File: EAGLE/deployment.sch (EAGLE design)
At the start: 7 parts, among them J1 1935161, J2 1935161, J3 1935161, Q1 100V 14A

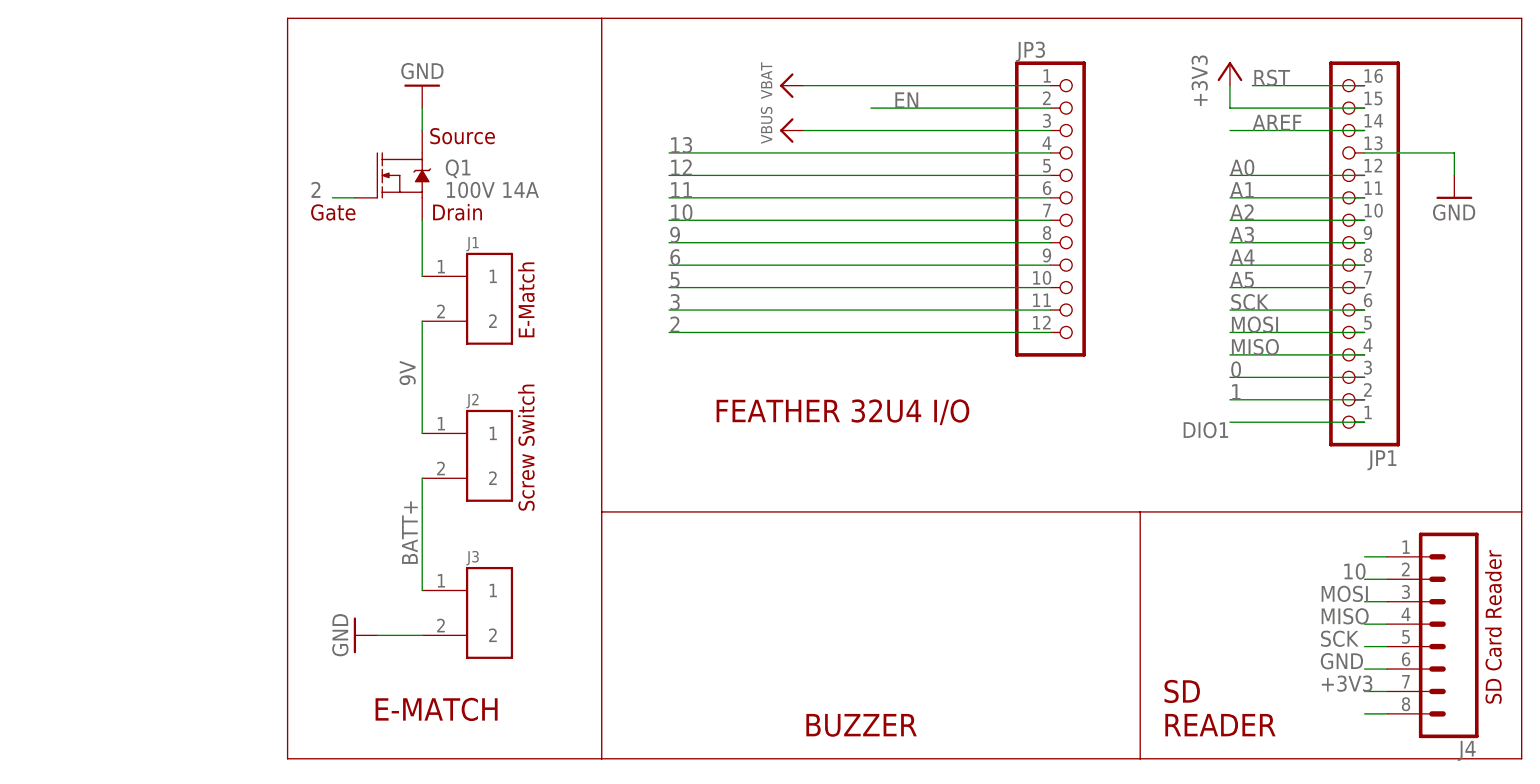
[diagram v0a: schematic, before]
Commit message: Added nichrome wire circuit to deployment schematic
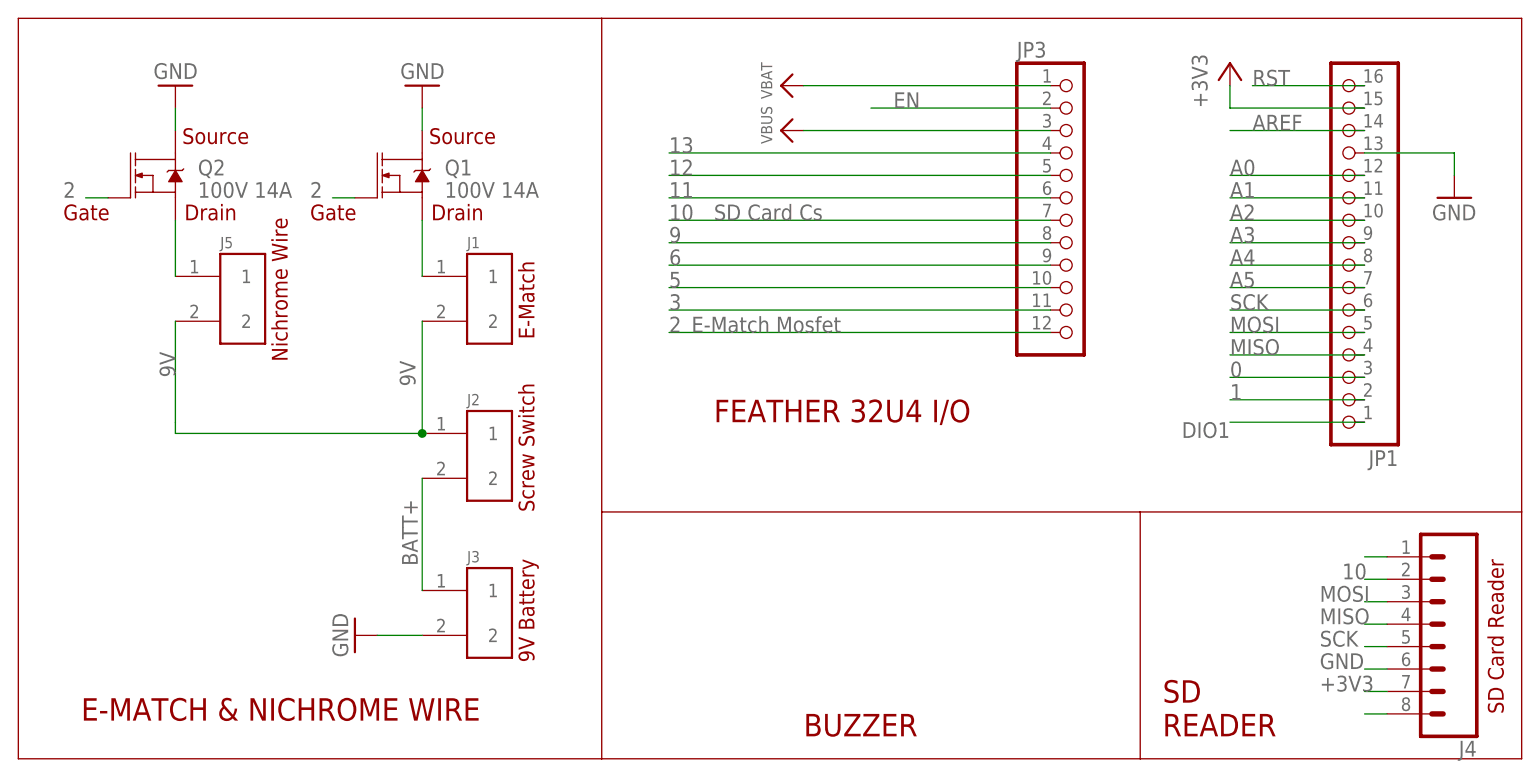
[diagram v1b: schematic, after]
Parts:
- added J5: 1935161, 1935161:1935161
- added Q2: 100V 14A, SparkFun-DiscreteSemi:MOSFET-NCH-FQP30N06L
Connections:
- new net N$2: J5.1, Q2.S
- net 2: now also Q2.G
- net 9V: now also J5.2
- net GND: now also Q2.D
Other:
- note added: "9V Battery"
- note added: "E-MATCH & NICHROME WIRE"
- note added: "E-Match Mosfet"
- note added: "Nichrome Wire"
- note added: "SD Card Cs"
- note removed: "E-MATCH"
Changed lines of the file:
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@@
 <part name="GND2" library="supply1" deviceset="GND" device=""/>
 <part name="J4" library="SparkFun-Connectors" library_urn="urn:adsk.eagle:library:513" deviceset="CONN_08" device="&quot;" package3d_urn="urn:adsk.eagle:package:38138/1"/>
+<part name="Q2" library="SparkFun-DiscreteSemi" library_urn="urn:adsk.eagle:library:514" deviceset="MOSFET-NCH" device="-FQP30N06L" package3d_urn="urn:adsk.eagle:package:38447/1" value="100V 14A"/>
+<part name="J5" library="1935161" deviceset="1935161" device="" value=""/>
+<part name="GND3" library="supply1" deviceset="GND" device=""/>
 </parts>
 <sheets>
@@
 <text x="58.42" y="55.118" size="1.778" layer="94" rot="R90">E-Match</text>
 <text x="58.42" y="35.56" size="1.778" layer="94" rot="R90">Screw Switch</text>
-<text x="167.894" y="13.716" size="1.778" layer="94" rot="R90">SD Card Reader</text>
+<text x="168.148" y="12.7" size="1.778" layer="94" rot="R90">SD Card Reader</text>
 <wire x1="170.18" y1="35.56" x2="170.18" y2="7.62" width="0.1524" layer="94"/>
 <wire x1="170.18" y1="7.62" x2="127" y2="7.62" width="0.1524" layer="94"/>
 <wire x1="127" y1="7.62" x2="127" y2="35.56" width="0.1524" layer="94"/>
 <wire x1="127" y1="7.62" x2="66.04" y2="7.62" width="0.1524" layer="94"/>
-<wire x1="66.04" y1="7.62" x2="30.48" y2="7.62" width="0.1524" layer="94"/>
-<wire x1="30.48" y1="7.62" x2="30.48" y2="91.44" width="0.1524" layer="94"/>
-<wire x1="30.48" y1="91.44" x2="66.04" y2="91.44" width="0.1524" layer="94"/>
+<wire x1="66.04" y1="7.62" x2="0" y2="7.62" width="0.1524" layer="94"/>
+<wire x1="0" y1="7.62" x2="0" y2="91.44" width="0.1524" layer="94"/>
+<wire x1="0" y1="91.44" x2="66.04" y2="91.44" width="0.1524" layer="94"/>
 <wire x1="66.04" y1="35.56" x2="66.04" y2="7.62" width="0.1524" layer="94"/>
-<text x="40.132" y="11.938" size="2.54" layer="94">E-MATCH</text>
+<text x="7.112" y="11.938" size="2.54" layer="94">E-MATCH &amp; NICHROME WIRE</text>
 <text x="78.74" y="45.72" size="2.54" layer="94">FEATHER 32U4 I/O</text>
 <text x="129.54" y="10.16" size="2.54" layer="94">SD
 READER</text>
 <text x="88.9" y="10.16" size="2.54" layer="94">BUZZER</text>
+<text x="58.42" y="18.542" size="1.778" layer="94" rot="R90">9V Battery</text>
+<text x="76.2" y="55.88" size="1.778" layer="95">E-Match Mosfet</text>
+<text x="78.74" y="68.58" size="1.778" layer="95">SD Card Cs</text>
+<text x="5.08" y="68.58" size="1.778" layer="94">Gate</text>
+<text x="18.542" y="77.216" size="1.778" layer="94">Source</text>
+<text x="18.796" y="68.58" size="1.778" layer="94">Drain</text>
+<text x="30.48" y="52.578" size="1.778" layer="94" rot="R90">Nichrome Wire</text>
 </plain>
 <instances>
@@
 <attribute name="VALUE" x="165.1" y="35.306" size="1.778" layer="96" font="vector" rot="R180"/>
 <attribute name="NAME" x="165.1" y="9.652" size="1.778" layer="95" font="vector" rot="R180"/>
+</instance>
+<instance part="Q2" gate="NMOS" x="15.24" y="73.66" smashed="yes">
+<attribute name="NAME" x="20.32" y="73.66" size="1.778" layer="95" font="vector"/>
+<attribute name="VALUE" x="20.32" y="71.12" size="1.778" layer="96" font="vector"/>
+</instance>
+<instance part="J5" gate="G$1" x="25.4" y="59.69" smashed="yes">
+<attribute name="NAME" x="22.85451875" y="65.417340625" size="1.272740625" layer="95"/>
+<attribute name="VALUE" x="22.85191875" y="52.04576875" size="1.274040625" layer="96"/>
+</instance>
+<instance part="GND3" gate="1" x="17.78" y="83.82" smashed="yes" rot="R180">
+<attribute name="VALUE" x="20.32" y="86.36" size="1.778" layer="96" rot="R180"/>
 </instance>
 </instances>
@@
 <label x="147.32" y="17.78" size="1.778" layer="95"/>
 </segment>
+<segment>
+<pinref part="GND3" gate="1" pin="GND"/>
+<pinref part="Q2" gate="NMOS" pin="D"/>
+<wire x1="17.78" y1="81.28" x2="17.78" y2="78.74" width="0.1524" layer="91"/>
+</segment>
 </net>
 <net name="MOSI" class="0">
@@
 <wire x1="38.1" y1="71.12" x2="35.56" y2="71.12" width="0.1524" layer="91"/>
 <label x="33.02" y="71.12" size="1.778" layer="95"/>
+</segment>
+<segment>
+<pinref part="Q2" gate="NMOS" pin="G"/>
+<wire x1="10.16" y1="71.12" x2="7.62" y2="71.12" width="0.1524" layer="91"/>
+<label x="5.08" y="71.12" size="1.778" layer="95"/>
 </segment>
 </net>
@@
 <wire x1="45.72" y1="57.15" x2="45.72" y2="44.45" width="0.1524" layer="91"/>
 <label x="44.958" y="49.784" size="1.778" layer="95" rot="R90"/>
+<pinref part="J5" gate="G$1" pin="2"/>
+<wire x1="17.78" y1="57.15" x2="17.78" y2="45.72" width="0.1524" layer="91"/>
+<wire x1="45.72" y1="44.45" x2="17.78" y2="44.45" width="0.1524" layer="91"/>
+<wire x1="17.78" y1="44.45" x2="17.78" y2="45.72" width="0.1524" layer="91"/>
+<junction x="45.72" y="44.45"/>
+<label x="17.78" y="50.8" size="1.778" layer="95" rot="R90"/>
 </segment>
 </net>
@@
 </segment>
 </net>
+<net name="N$2" class="0">
+<segment>
+<pinref part="J5" gate="G$1" pin="1"/>
+<pinref part="Q2" gate="NMOS" pin="S"/>
+<wire x1="17.78" y1="62.23" x2="17.78" y2="68.58" width="0.1524" layer="91"/>
+</segment>
+</net>
